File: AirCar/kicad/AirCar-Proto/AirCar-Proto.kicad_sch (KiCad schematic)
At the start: 21 parts, among them J1 Conn_01x05, J3 Conn_01x06, J4 PJ-102A, SW2 SW_SPDT, U1 Pico, U2 LDL212PU50R, U3 TXU0104BQAR

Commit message: Gerbers for initial proto
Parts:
- U3: Vendor (none) -> 296-TXU0104BQARTR-ND
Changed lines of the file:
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@@
       (effects (font (size 1.27 1.27) italic) hide)
+    )
+    (property "Vendor" "296-TXU0104BQARTR-ND" (at 99.06 63.5 0)
+      (effects (font (size 1.27 1.27)) hide)
     )
     (pin "1")

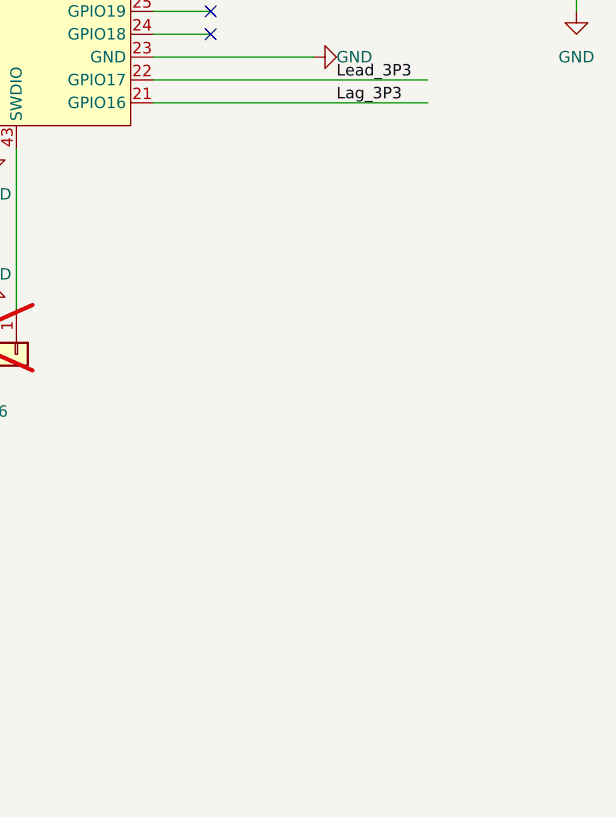
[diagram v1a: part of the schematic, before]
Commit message: add pin headers and BOM
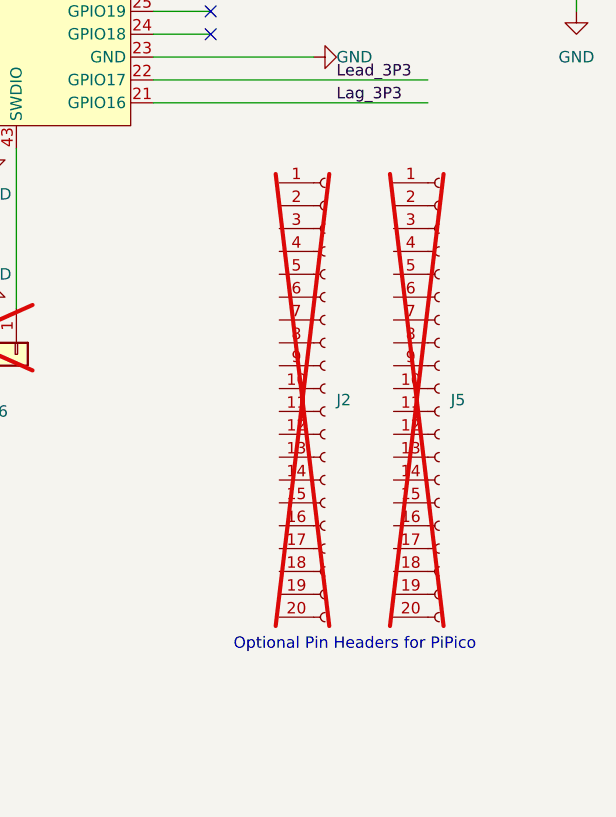
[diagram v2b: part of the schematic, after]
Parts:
- added J2, J5: Conn_01x20_Socket, Connector_PinHeader_2.54mm:PinHeader_1x20_P2.54mm_Vertical, symbol Connector:Conn_01x20_Socket
- D1: Vendor (none) -> CRS01QCT-ND
- J1: Vendor (none) -> WM4903-ND
- Reset1, USER1: Digikey (none) -> 450-1650-ND; Vendor (none) -> 450-1650-ND
- SW2: Vendor (none) -> 360-2131-ND
- U1: Vendor (none) -> 2648-SC0915TR-ND
- U2: Digikey (none) -> 497-16897-2-ND; Vendor (none) -> 497-16897-2-ND
- U3: Digikey (none) -> 296-TXU0104BQARTR-ND
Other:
- note added: "Optional Pin Headers for PiPico"
